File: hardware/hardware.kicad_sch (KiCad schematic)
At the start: 95 parts, among them IC1 TAS5760LDAPR, J1 GMC020080HR, J2 Conn_01x04, J3 Conn_01x04, SW1 SW_Push, SW2 SW_Push, SW3 SW_Push, SW5 SW_Push, U1 TPS563200, U2 ESP32-S3, Y1 40MHz, Y2 ABS07-166-32.768KHZ-T

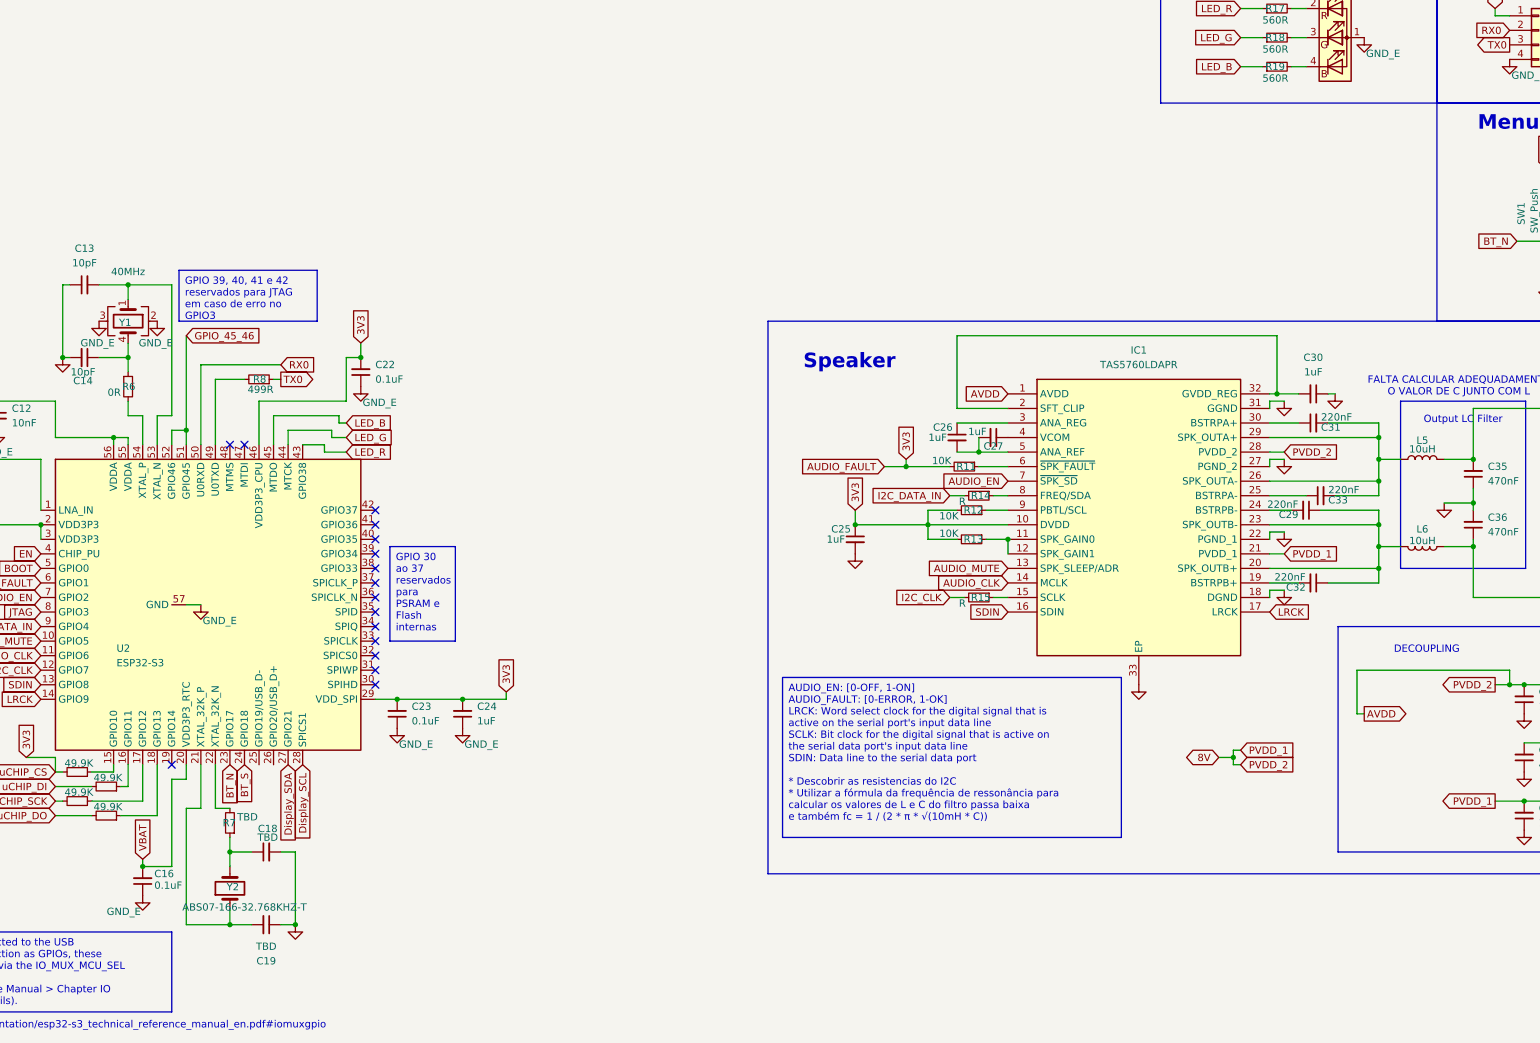
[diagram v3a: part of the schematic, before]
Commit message: esquemático com JTAG usb adicionada; preferi deixar o monitor numa i2c separada da i2c do amplificador de audio - para nao correr o risco de ao diminuir o volume buggar a tela
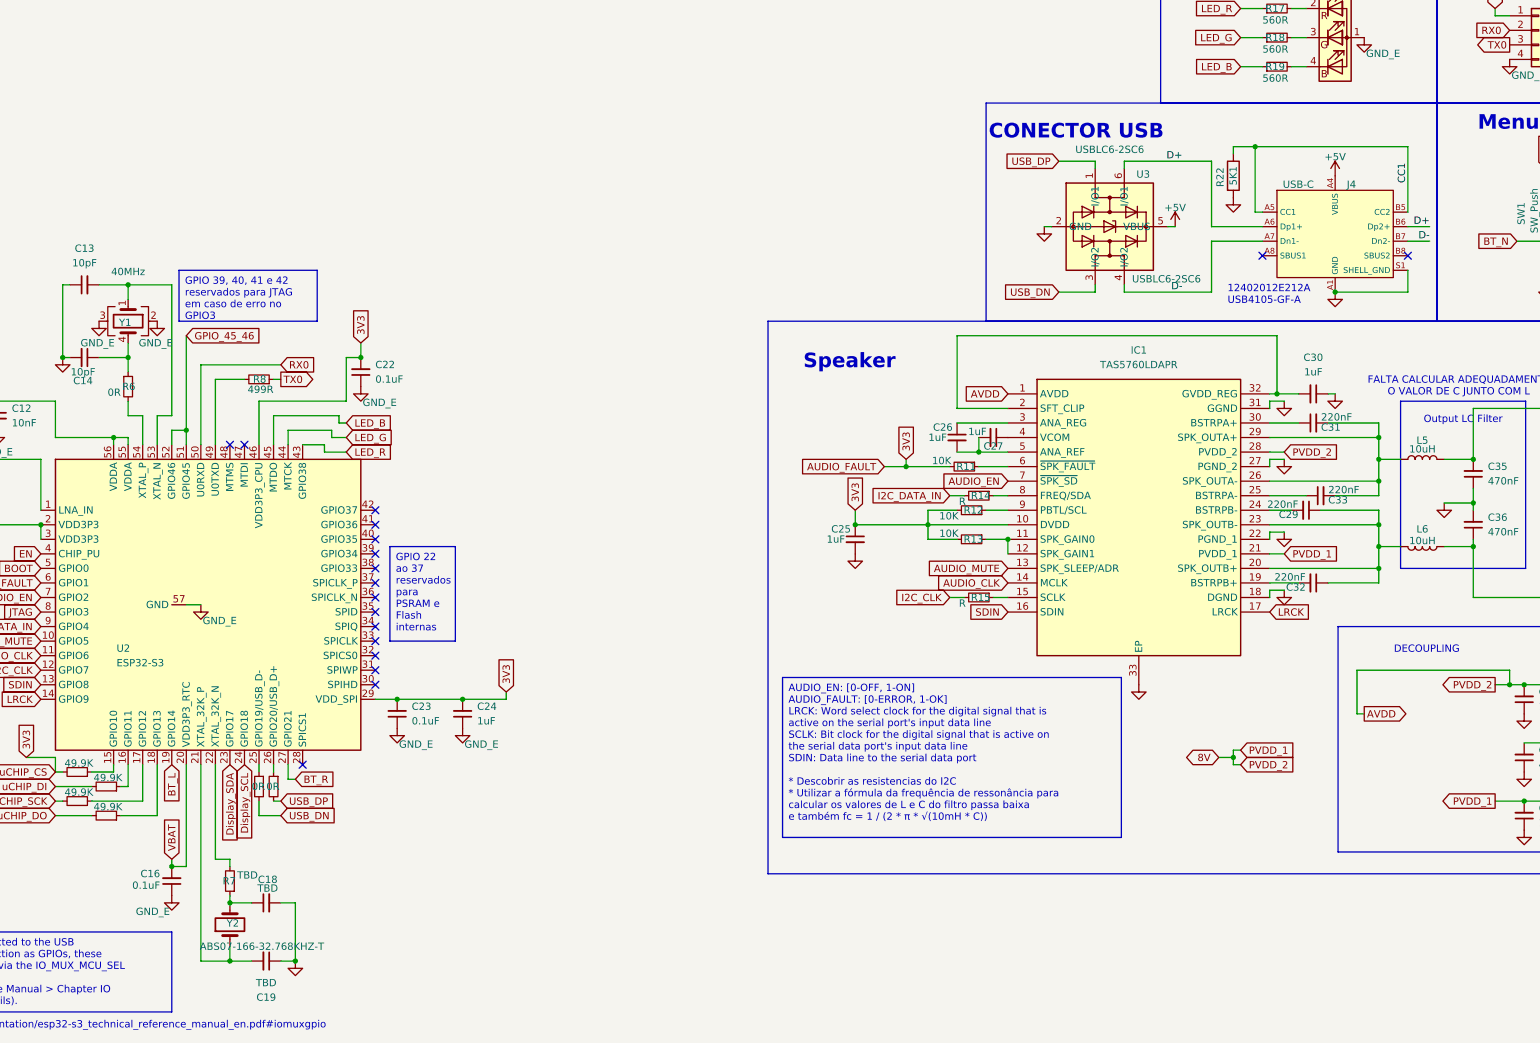
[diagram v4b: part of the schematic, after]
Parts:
- added J4: USB-C, Connector_USB:USB_C_Receptacle_XKB_U262-16XN-4BVC11, symbol Rastreador_Library:USB-C
- added R22: 5K1, Resistor_SMD:R_0402_1005Metric, symbol Device:R
- added R26, R28: 0R, Resistor_SMD:R_0402_1005Metric, symbol Device:R_Small
- added U3: USBLC6-2SC6, Package_TO_SOT_SMD:TSOT-23-6_HandSoldering, symbol Rastreador_Library:USBLC6-CUSTOM
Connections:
- net BT_N: no longer U2.23 (GPIO17)
- net BT_S: no longer U2.24 (GPIO18)
- net Display_SCL: now also U2.24 (GPIO18); no longer U2.28 (SPICS1)
- net Display_SDA: now also U2.23 (GPIO17); no longer U2.27 (GPIO21)
- net GND: now also J4.A1 (GND), J4.A12 (GND), J4.B1 (GND), J4.B12 (GND), J4.S1 (SHELL_GND), R22.2, U3.2 (GND)
- net BT_L: now reaches U2.19 (GPIO14)
- net at U2.25 (GPIO19/USB_D-): now also R26.1
- net at U2.26 (GPIO20/USB_D+): now also R28.1
- new net +5V: J4.A4 (VBUS), J4.A9 (VBUS), J4.B4 (VBUS), J4.B9 (VBUS), U3.5 (VBUS)
- new net BT_R: U2.27 (GPIO21)
- new net CC1: J4.A5 (CC1), J4.B5 (CC2), R22.1
- new net D+: J4.A6 (Dp1+), J4.B6 (Dp2+), U3.6 (I/O1)
- new net D-: J4.A7 (Dn1-), J4.B7 (Dn2-), U3.4 (I/O2)
- new net USB_DN: R26.2, U3.3 (I/O2)
- new net USB_DP: R28.2, U3.1 (I/O1)
- no-connect marks 21 -> 23
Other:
- note added: "12402012E212A USB4105-GF-A"
- note added: "CONECTOR USB"
- moved on the sheet: C16, C18, C19, R7, Y2

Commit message: sound components placed - there were some differences between layout and schematic on the amplifier documentation. They are emphasized by squares on schematic
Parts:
- removed JP1, JP2: SolderJumper_2_Open, Jumper:SolderJumper-2_P1.3mm_Open_RoundedPad1.0x1.5mm, symbol Jumper:SolderJumper_2_Open
- added C42, C46: 1uF, Capacitor_SMD:C_0402_1005Metric, symbol Device:C_Small
- added R29: 47R, Resistor_SMD:R_0201_0603Metric_Pad0.64x0.40mm_HandSolder, symbol Device:R_Small
- added R30: 10K, Resistor_SMD:R_0201_0603Metric_Pad0.64x0.40mm_HandSolder, symbol Device:R_Small
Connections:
- net BT_N is gone; now on net BT_L: C28.1, R16.1, SW1.2
- net BT_S is gone; now on net BT_R: C34.1, R20.1, SW2.2
- net +8V: now also C42.2
- net 3V3: now also R11.1; no longer R11.2, U2.6 (GPIO1)
- net GND: now also C42.1, C46.2, R29.2
- net at C40.2: now also JP3.1 (A), R23.1
- net at C30.2, IC1.32 (GVDD_REG): now also R30.2; no longer IC1.2 (SFT_CLIP)
- net AUDIO_FAULT: now reaches IC1.6 (~{SPK_FAULT})
- net AUDIO_FAULT: now also R11.2, U2.6 (GPIO1); no longer R11.1
- net at JP4.2 (B), R24.2: now also C41.1
- new net: C46.1, IC1.2 (SFT_CLIP), R29.1, R30.1
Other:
- moved on the sheet: JP3, JP4, R11

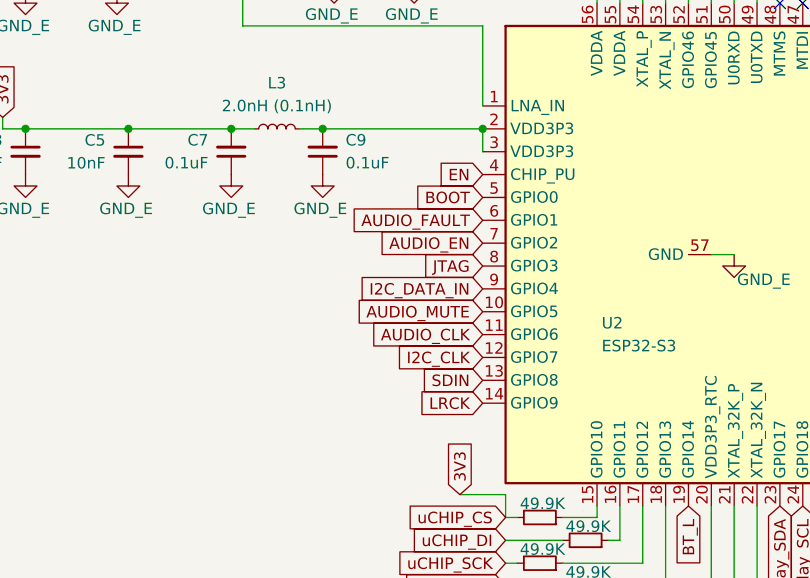
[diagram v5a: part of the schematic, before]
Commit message: roteamentos do amplificador, perifericos agrupados
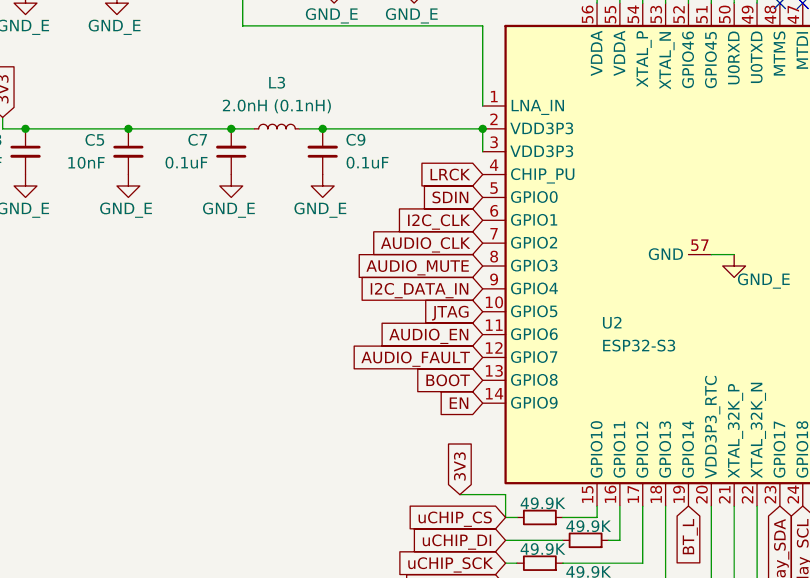
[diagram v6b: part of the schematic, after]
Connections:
- net AUDIO_CLK: now also U2.7 (GPIO2); no longer U2.11 (GPIO6)
- net AUDIO_EN: now also U2.11 (GPIO6); no longer U2.7 (GPIO2)
- net AUDIO_FAULT: now also U2.12 (GPIO7); no longer U2.6 (GPIO1)
- net AUDIO_MUTE: now also U2.8 (GPIO3); no longer U2.10 (GPIO5)
- net BOOT: now also U2.13 (GPIO8); no longer U2.5 (GPIO0)
- net EN: now also U2.14 (GPIO9); no longer U2.4 (CHIP_PU)
- net I2C_CLK: now also U2.6 (GPIO1); no longer U2.12 (GPIO7)
- net JTAG: now also U2.10 (GPIO5); no longer U2.8 (GPIO3)
- net LRCK: now also U2.4 (CHIP_PU); no longer U2.14 (GPIO9)
- net SDIN: now also U2.5 (GPIO0); no longer U2.13 (GPIO8)
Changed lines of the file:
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@@
 	(global_label "LRCK"
 		(shape input)
-		(at 99.06 203.2 180)
-		(fields_autoplaced yes)
-		(effects
-			(font
-				(size 1.27 1.27)
-			)
-			(justify right)
-		)
-		(property "Intersheetrefs" "${INTERSHEET_REFS}"
-			(at 91.2367 203.2 0)
+		(at 99.06 177.8 180)
+		(fields_autoplaced yes)
+		(effects
+			(font
+				(size 1.27 1.27)
+			)
+			(justify right)
+		)
+		(property "Intersheetrefs" "${INTERSHEET_REFS}"
+			(at 91.2367 177.8 0)
 			(effects
 				(font
@@
 	(global_label "SDIN"
 		(shape input)
-		(at 99.06 200.66 180)
-		(fields_autoplaced yes)
-		(effects
-			(font
-				(size 1.27 1.27)
-			)
-			(justify right)
-		)
-		(property "Intersheetrefs" "${INTERSHEET_REFS}"
-			(at 91.66 200.66 0)
+		(at 99.06 180.34 180)
+		(fields_autoplaced yes)
+		(effects
+			(font
+				(size 1.27 1.27)
+			)
+			(justify right)
+		)
+		(property "Intersheetrefs" "${INTERSHEET_REFS}"
+			(at 91.66 180.34 0)
 			(effects
 				(font
@@
 	(global_label "I2C_CLK"
 		(shape input)
-		(at 99.06 198.12 180)
-		(fields_autoplaced yes)
-		(effects
-			(font
-				(size 1.27 1.27)
-			)
-			(justify right)
-		)
-		(property "Intersheetrefs" "${INTERSHEET_REFS}"
-			(at 88.4548 198.12 0)
+		(at 99.06 182.88 180)
+		(fields_autoplaced yes)
+		(effects
+			(font
+				(size 1.27 1.27)
+			)
+			(justify right)
+		)
+		(property "Intersheetrefs" "${INTERSHEET_REFS}"
+			(at 88.4548 182.88 0)
 			(effects
 				(font
@@
 	(global_label "AUDIO_CLK"
 		(shape input)
-		(at 99.06 195.58 180)
-		(fields_autoplaced yes)
-		(effects
-			(font
-				(size 1.27 1.27)
-			)
-			(justify right)
-		)
-		(property "Intersheetrefs" "${INTERSHEET_REFS}"
-			(at 85.9147 195.58 0)
+		(at 99.06 185.42 180)
+		(fields_autoplaced yes)
+		(effects
+			(font
+				(size 1.27 1.27)
+			)
+			(justify right)
+		)
+		(property "Intersheetrefs" "${INTERSHEET_REFS}"
+			(at 85.9147 185.42 0)
 			(effects
 				(font
@@
 	(global_label "BOOT"
 		(shape input)
-		(at 99.06 180.34 180)
-		(fields_autoplaced yes)
-		(effects
-			(font
-				(size 1.27 1.27)
-			)
-			(justify right)
-		)
-		(property "Intersheetrefs" "${INTERSHEET_REFS}"
-			(at 91.1762 180.34 0)
+		(at 99.06 200.66 180)
+		(fields_autoplaced yes)
+		(effects
+			(font
+				(size 1.27 1.27)
+			)
+			(justify right)
+		)
+		(property "Intersheetrefs" "${INTERSHEET_REFS}"
+			(at 91.1762 200.66 0)
 			(effects
 				(font
@@
 	(global_label "AUDIO_EN"
 		(shape input)
-		(at 99.06 185.42 180)
-		(fields_autoplaced yes)
-		(effects
-			(font
-				(size 1.27 1.27)
-			)
-			(justify right)
-		)
-		(property "Intersheetrefs" "${INTERSHEET_REFS}"
-			(at 87.0033 185.42 0)
+		(at 99.06 195.58 180)
+		(fields_autoplaced yes)
+		(effects
+			(font
+				(size 1.27 1.27)
+			)
+			(justify right)
+		)
+		(property "Intersheetrefs" "${INTERSHEET_REFS}"
+			(at 87.0033 195.58 0)
 			(effects
 				(font
@@
 	(global_label "EN"
 		(shape input)
-		(at 99.06 177.8 180)
-		(fields_autoplaced yes)
-		(effects
-			(font
-				(size 1.27 1.27)
-			)
-			(justify right)
-		)
-		(property "Intersheetrefs" "${INTERSHEET_REFS}"
-			(at 93.5953 177.8 0)
+		(at 99.06 203.2 180)
+		(fields_autoplaced yes)
+		(effects
+			(font
+				(size 1.27 1.27)
+			)
+			(justify right)
+		)
+		(property "Intersheetrefs" "${INTERSHEET_REFS}"
+			(at 93.5953 203.2 0)
 			(effects
 				(font
@@
 	(global_label "AUDIO_FAULT"
 		(shape input)
-		(at 99.06 182.88 180)
-		(fields_autoplaced yes)
-		(effects
-			(font
-				(size 1.27 1.27)
-			)
-			(justify right)
-		)
-		(property "Intersheetrefs" "${INTERSHEET_REFS}"
-			(at 83.9794 182.88 0)
+		(at 99.06 198.12 180)
+		(fields_autoplaced yes)
+		(effects
+			(font
+				(size 1.27 1.27)
+			)
+			(justify right)
+		)
+		(property "Intersheetrefs" "${INTERSHEET_REFS}"
+			(at 83.9794 198.12 0)
 			(effects
 				(font
@@
 	(global_label "JTAG"
 		(shape input)
+		(at 99.06 193.04 180)
+		(fields_autoplaced yes)
+		(effects
+			(font
+				(size 1.27 1.27)
+			)
+			(justify right)
+		)
+		(property "Intersheetrefs" "${INTERSHEET_REFS}"
+			(at 91.781 193.04 0)
+			(effects
+				(font
+					(size 1.27 1.27)
+				)
+				(justify right)
+				(hide yes)
+			)
+		)
+	)
+	(global_label "3V3"
+		(shape input)
+		(at 154.94 140.97 90)
+		(fields_autoplaced yes)
+		(effects
+			(font
+				(size 1.27 1.27)
+			)
+			(justify left)
+		)
+		(property "Intersheetrefs" "${INTERSHEET_REFS}"
+			(at 154.94 134.4772 90)
+			(effects
+				(font
+					(size 1.27 1.27)
+				)
+				(justify left)
+				(hide yes)
+			)
+		)
+	)
+	(global_label "AUDIO_MUTE"
+		(shape input)
 		(at 99.06 187.96 180)
 		(fields_autoplaced yes)
@@
 		)
 		(property "Intersheetrefs" "${INTERSHEET_REFS}"
-			(at 91.781 187.96 0)
-			(effects
-				(font
-					(size 1.27 1.27)
-				)
-				(justify right)
-				(hide yes)
-			)
-		)
-	)
-	(global_label "3V3"
-		(shape input)
-		(at 154.94 140.97 90)
-		(fields_autoplaced yes)
-		(effects
-			(font
-				(size 1.27 1.27)
-			)
-			(justify left)
-		)
-		(property "Intersheetrefs" "${INTERSHEET_REFS}"
-			(at 154.94 134.4772 90)
-			(effects
-				(font
-					(size 1.27 1.27)
-				)
-				(justify left)
-				(hide yes)
-			)
-		)
-	)
-	(global_label "AUDIO_MUTE"
-		(shape input)
-		(at 99.06 193.04 180)
-		(fields_autoplaced yes)
-		(effects
-			(font
-				(size 1.27 1.27)
-			)
-			(justify right)
-		)
-		(property "Intersheetrefs" "${INTERSHEET_REFS}"
-			(at 84.5843 193.04 0)
-			(effects
-				(font
+			(at 84.5843 187.96 0)
+			(effects
+				(font

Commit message: usb
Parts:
- U3: footprint Package_TO_SOT_SMD:TSOT-23-6_HandSoldering -> SamacSys_Parts:SOT95P280X145-6N
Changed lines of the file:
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@@
 			)
 		)
-		(property "Footprint" "Package_TO_SOT_SMD:TSOT-23-6_HandSoldering"
+		(property "Footprint" "SamacSys_Parts:SOT95P280X145-6N"
 			(at 293.37 134.62 0)
 			(effects

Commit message: desacoplamento
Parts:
- removed Y1: 40MHz, Crystal:Crystal_SMD_2520-4Pin_2.5x2.0mm, symbol Device:Crystal_GND23
- added Y1: ECS-400-10-36B2-CKM-TR, Crystal:Crystal_SMD_2520-4Pin_2.5x2.0mm, symbol Device:Crystal_GND24
- J1: value GMC020080HR -> 798-DM3D-SF; symbol GMC020080HR:GMC020080HR -> Connector:Micro_SD_Card_Det_Hirose_DM3AT
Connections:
- net 3V3: now also J1.2 (DAT3/CD); no longer J1.1 (CD/DAT3)
- net GND_E: now also J1.11 (SHIELD), Y1.2, Y1.4; no longer J1.MP1 (GND_1), J1.MP2 (GND_2), J1.MP4 (WP_PIN), J1.MP5 (GND_3), J1.MP6 (GND_4)
- net uCHIP_DI: now also J1.3 (CMD); no longer J1.2 (CMD)
- net at C13.2, U2.53 (XTAL_N): now also Y1.3
- net at C14.1, R6.1: now also Y1.1
- no-connect marks 23 -> 22
